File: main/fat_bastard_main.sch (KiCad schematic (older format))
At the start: 51 parts, among them J1 INPUT, J2 TO_LD_12V, J3 TO_LD_IN, J4 TO_LD_GAIN, J5 TO_LD_OUT, J6 12V_IN, J8 FOOTSW, J9 OUTPUT, K1 FINDER-30.22, U1 OPA2134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

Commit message: [main] First version of the main PCB
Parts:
- added R17: 1M, Resistor_THT:R_Axial_DIN0309_L9.0mm_D3.2mm_P12.70mm_Horizontal, symbol Device:R
- C1, C12, C14, C3, C4, C5, C8, C9: footprint Capacitor_THT:C_Rect_L7.0mm_W2.5mm_P5.00mm -> Capacitor_THT:C_Rect_L7.2mm_W3.0mm_P5.00mm_FKS2_FKP2_MKS2_MKP2
- C10: footprint (none) -> Capacitor_THT:CP_Radial_D8.0mm_P3.80mm
- C11, C2, C6: footprint Capacitor_THT:C_Rect_L7.0mm_W2.5mm_P5.00mm -> Capacitor_THT:C_Rect_L10.0mm_W5.0mm_P5.00mm_P7.50mm
- C7: footprint (none) -> Capacitor_THT:CP_Radial_D10.0mm_P5.00mm
- D1, D2: footprint (none) -> Diode_THT:D_DO-41_SOD81_P7.62mm_Horizontal
- D3: footprint (none) -> LED_THT:LED_D3.0mm_Horizontal_O3.81mm_Z6.0mm
- R1, R10, R11, R12, R13, R14, R15, R16, R2, R3, R4, R5, R6, R7, R8, R9: footprint Resistor_THT:R_Axial_DIN0207_L6.3mm_D2.5mm_P7.62mm_Horizontal -> Resistor_THT:R_Axial_DIN0309_L9.0mm_D3.2mm_P12.70mm_Horizontal
- U1, U2, U3: footprint (none) -> Package_DIP:DIP-8_W7.62mm_Socket_LongPads
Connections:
- net GNDS: now also R17.2
- net at K1.11, U3.3 (+): now also R17.1

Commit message: [main] Attenuate lead channel & improve buffering + final PCB
Lead channel has a high output level, while the signal level after the
Depth control is quite low. Therfore, we need to attenuate the lead
channel before trying to mix in the signal coming from the Depth pot.

Additionnally, the output buffer is changed to a make-up gain stage.

With these changes in mind, the PCB design has been completed.
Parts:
- removed C11: 500p, Capacitor_THT:C_Rect_L10.0mm_W5.0mm_P5.00mm_P7.50mm, symbol Device:C
- added D4: PWR, LED_THT:LED_D3.0mm_Horizontal_O3.81mm_Z2.0mm, symbol Device:LED
- added R18: 1.8k, Resistor_THT:R_Axial_DIN0309_L9.0mm_D3.2mm_P12.70mm_Horizontal, symbol Device:R
- added R19: 47k, Resistor_THT:R_Axial_DIN0309_L9.0mm_D3.2mm_P12.70mm_Horizontal, symbol Device:R
- added R20: 10k, Resistor_THT:R_Axial_DIN0309_L9.0mm_D3.2mm_P12.70mm_Horizontal, symbol Device:R
- added R21: 1k, Resistor_THT:R_Axial_DIN0309_L9.0mm_D3.2mm_P12.70mm_Horizontal, symbol Device:R
- added R22: 4.7k, Resistor_THT:R_Axial_DIN0309_L9.0mm_D3.2mm_P12.70mm_Horizontal, symbol Device:R
- C1: value 1n -> 1.5n
- C12: value 100n -> 220n
- C15: footprint Capacitor_THT:C_Rect_L7.0mm_W2.5mm_P5.00mm -> Capacitor_THT:C_Rect_L7.2mm_W4.5mm_P5.00mm_FKS2_FKP2_MKS2_MKP2
- C2, C6: footprint Capacitor_THT:C_Rect_L10.0mm_W5.0mm_P5.00mm_P7.50mm -> Capacitor_THT:C_Disc_D10.5mm_W5.0mm_P5.00mm
- D3: value LED -> LEAD; footprint LED_THT:LED_D3.0mm_Horizontal_O3.81mm_Z6.0mm -> LED_THT:LED_D3.0mm_Horizontal_O6.35mm_Z10.0mm
- R10: value 8.2k -> 6.8k
- R13: value 470k -> 10k
- R14: value 470k -> 1M
- R15: value 3.3k -> 1.8k
- R9: value 10k -> 3.9k
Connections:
- net +12V: now also D4.2 (A)
- net GND: now also R18.2
- net GNDS: now also R19.2, R21.1
- net at C15.2, U3.6: now also R22.2; no longer U3.2 (-)
- net at U1.6 (-), U1.7: now also R20.1; no longer RV3.1
- net at U1.1, U1.2 (-): now also R13.2; no longer R13.1
- net at R14.1, U1.5 (+): now also R19.1; no longer R13.2
- new net: R13.1, R20.2, RV3.1
- new net: R21.2, R22.1, U3.2 (-)
- new net: D4.1 (K), R18.1
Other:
- moved on the sheet: J6, R13, R14, U1B

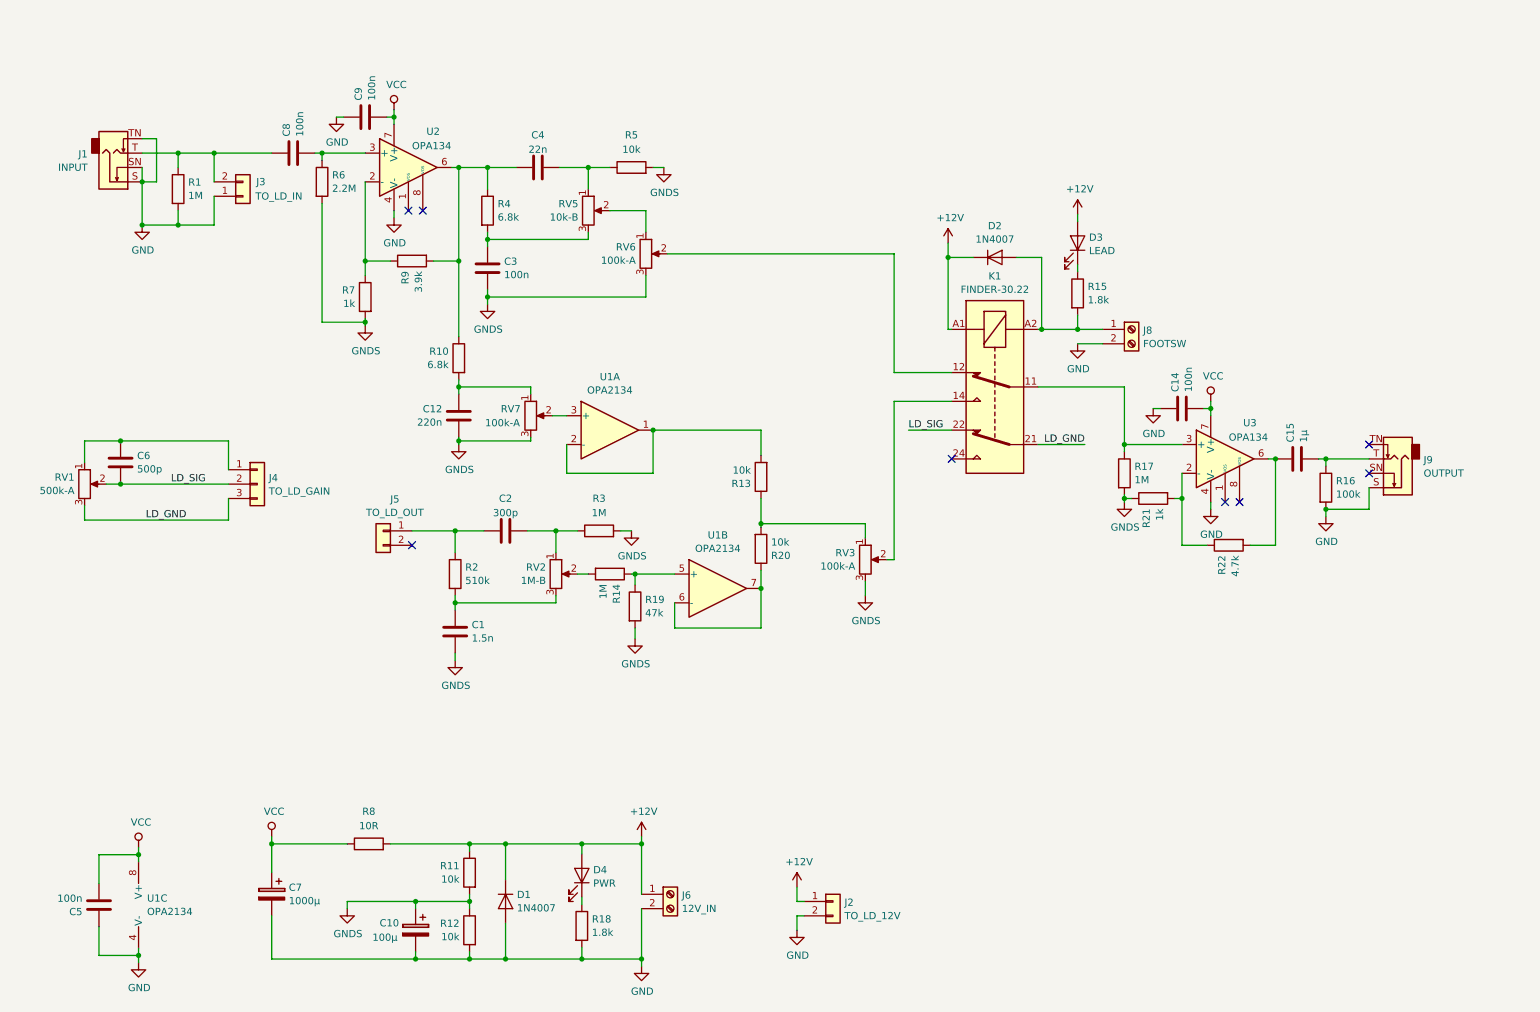
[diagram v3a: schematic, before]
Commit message: Make main-alt PCB the only main PCB
Signed-off-by: Arnaud Ferraris <arnaud.ferraris@gmail.com>
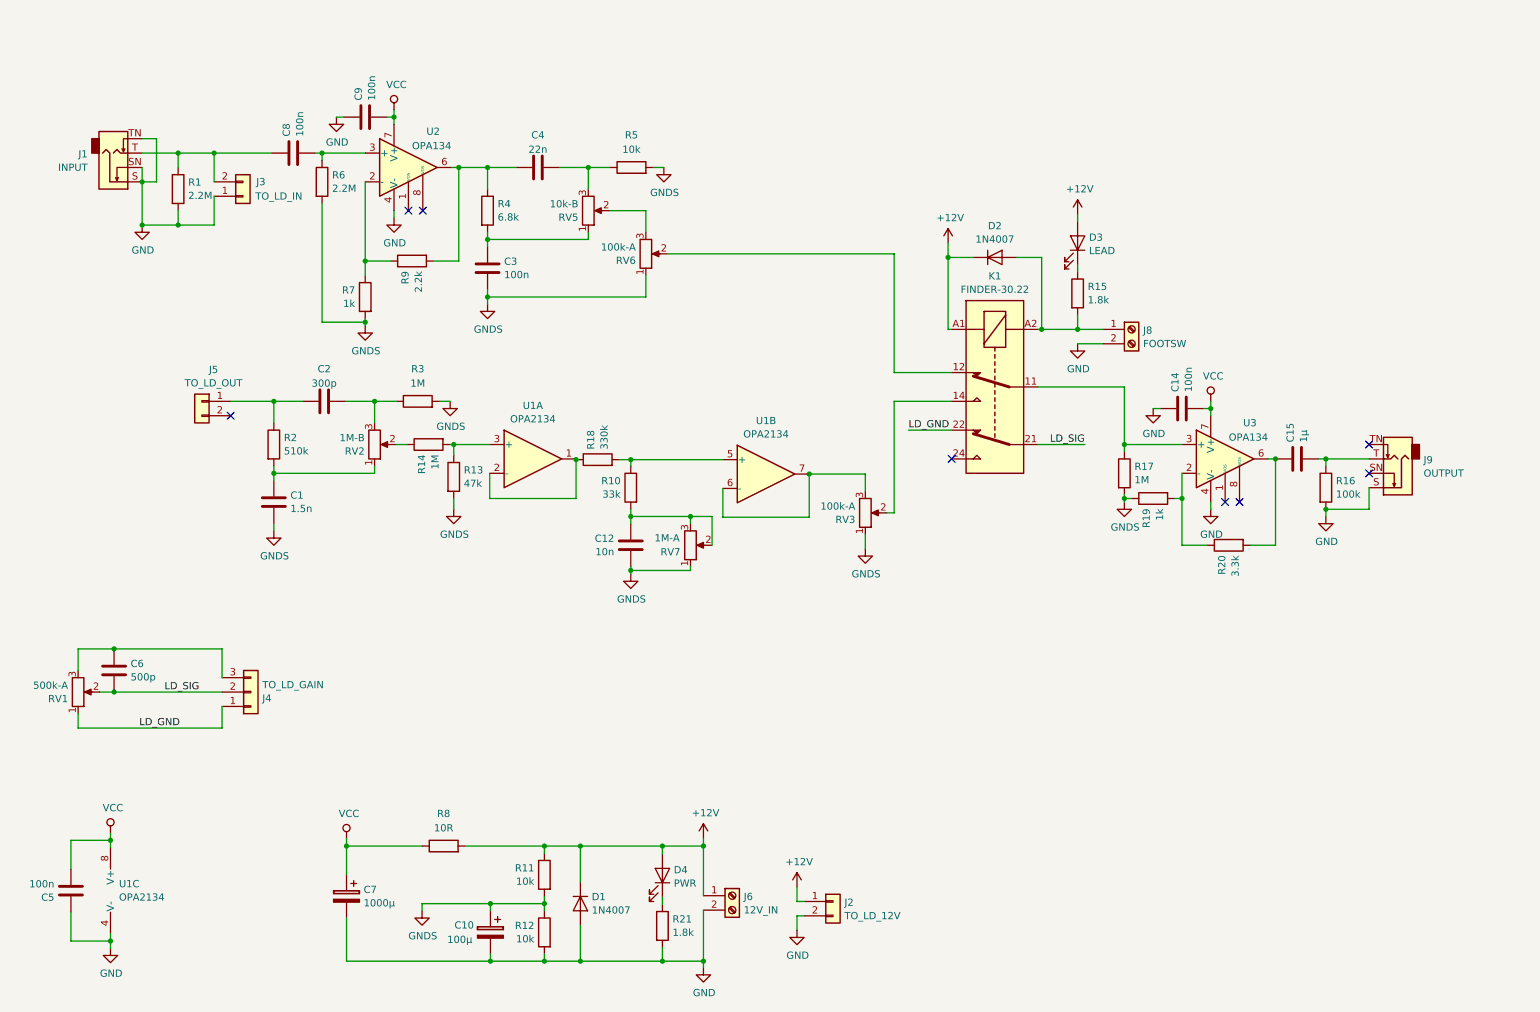
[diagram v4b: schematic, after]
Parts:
- removed R13, R20: 10k, Resistor_THT:R_Axial_DIN0309_L9.0mm_D3.2mm_P12.70mm_Horizontal, symbol Device:R
- added R21: 1.8k, Resistor_THT:R_Axial_DIN0309_L9.0mm_D3.2mm_P12.70mm_Horizontal, symbol Device:R
- C12: value 220n -> 10n
- R1: value 1M -> 2.2M
- R10: value 6.8k -> 33k
- R18: value 1.8k -> 330k
- R20: renamed from R22; value 4.7k -> 3.3k
- R9: value 3.9k -> 2.2k
- RV7: value 100k-A -> 1M-A
- renumbered R19 to R13, R21 to R19
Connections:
- net GND: now also R21.2; no longer R18.2
- net GNDS: now also RV3.1, RV6.1, RV7.1; no longer RV3.3, RV6.3, RV7.3
- net LD_GND: now also J4.1 (Pin_1), K1.22, RV1.1; no longer J4.3 (Pin_3), K1.21, RV1.3
- net LD_SIG: now also K1.21; no longer K1.22
- net at C4.2, R5.1: now also RV5.3; no longer RV5.1
- net at RV5.2: now also RV6.3; no longer RV6.1
- net at C3.2, R4.2: now also RV5.1; no longer RV5.3
- net at C4.1, R4.1, R9.2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: no longer R10.1
- net at C12.2, R10.2: now also RV7.2, RV7.3; no longer RV7.1
- net at C2.2, R3.1: now also RV2.3; no longer RV2.1
- net at R14.2: now also R13.1, U1.3 (+); no longer RV2.2
- net at C1.2, R2.2: now also RV2.1; no longer RV2.3
- net at R18.1: now also U1.1, U1.2 (-); no longer D4.1 (K)
- new net: C6.2, J4.3 (Pin_3), RV1.3
- new net: R14.1, RV2.2
- new net: RV3.3, U1.6 (-), U1.7
- new net: R10.1, R18.2, U1.5 (+)
- new net: D4.1 (K), R21.1
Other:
- moved on the sheet: C1, C10, C12, C2, C5, C6, C7, D1, J4, J5, J6, R10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

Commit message: Add bright cap, DI out & improve routing
* Add bright cap on clean channel
* Add DI out pin header
* Change connections to improve routing
* Connect pin 1 of each pin header & terminal block to GND for improved
  consistency
* Improve overall routing to avoid vias

Signed-off-by: Arnaud Ferraris <arnaud.ferraris@gmail.com>
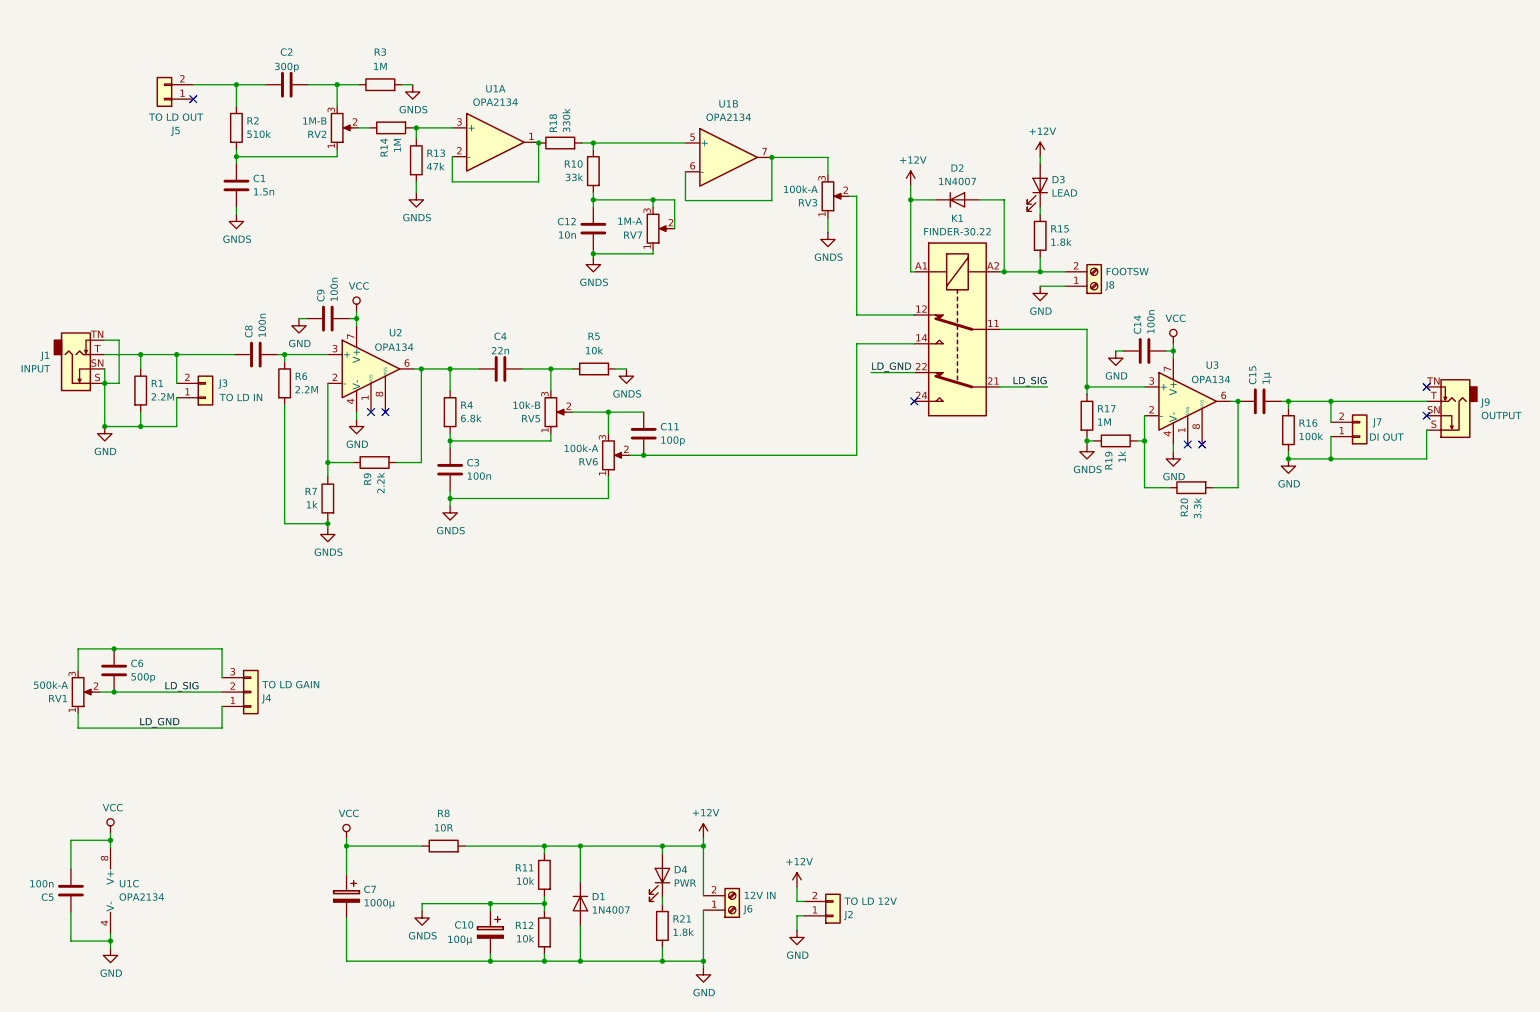
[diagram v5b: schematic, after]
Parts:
- added C11: 100p, Capacitor_THT:C_Disc_D10.5mm_W5.0mm_P5.00mm, symbol Device:C
- added J7: DI OUT, Connector_PinHeader_2.54mm:PinHeader_1x02_P2.54mm_Vertical, symbol Connector_Generic:Conn_01x02
- J2: value TO_LD_12V -> TO LD 12V
- J3: value TO_LD_IN -> TO LD IN
- J4: value TO_LD_GAIN -> TO LD GAIN
- J5: value TO_LD_OUT -> TO LD OUT
- J6: value 12V_IN -> 12V IN
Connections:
- net +12V: now also J2.2 (Pin_2), J6.2 (Pin_2); no longer J2.1 (Pin_1), J6.1 (Pin_1)
- net GND: now also J2.1 (Pin_1), J6.1 (Pin_1), J8.1 (Pin_1), J7.1 (Pin_1); no longer J2.2 (Pin_2), J6.2 (Pin_2), J8.2 (Pin_2)
- net at RV5.2, RV6.3: now also C11.2
- net at RV6.2: now also K1.14, C11.1; no longer K1.12
- net at D2.2 (A), K1.A2, R15.2: now also J8.2 (Pin_2); no longer J8.1 (Pin_1)
- net at RV3.2: now also K1.12; no longer K1.14
- net at C15.1, J9.T, R16.1: now also J7.2 (Pin_2)
- net at C2.1, R2.1: now also J5.2 (Pin_2); no longer J5.1 (Pin_1)
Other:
- moved on the sheet: C1, C12, C14, C15, C2, C3, C4, C8, C9, D2, D3, J1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
